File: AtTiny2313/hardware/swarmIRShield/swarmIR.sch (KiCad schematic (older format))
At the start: 32 parts, among them P1 CONN_2, P2 CONN_6, P3 CONN_2, P4 CONN_6, P5 CONN_2, P6 CONN_6, P7 CONN_2, P8 CONN_6, Q1 MOSFET_N, U1 TSOP1838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

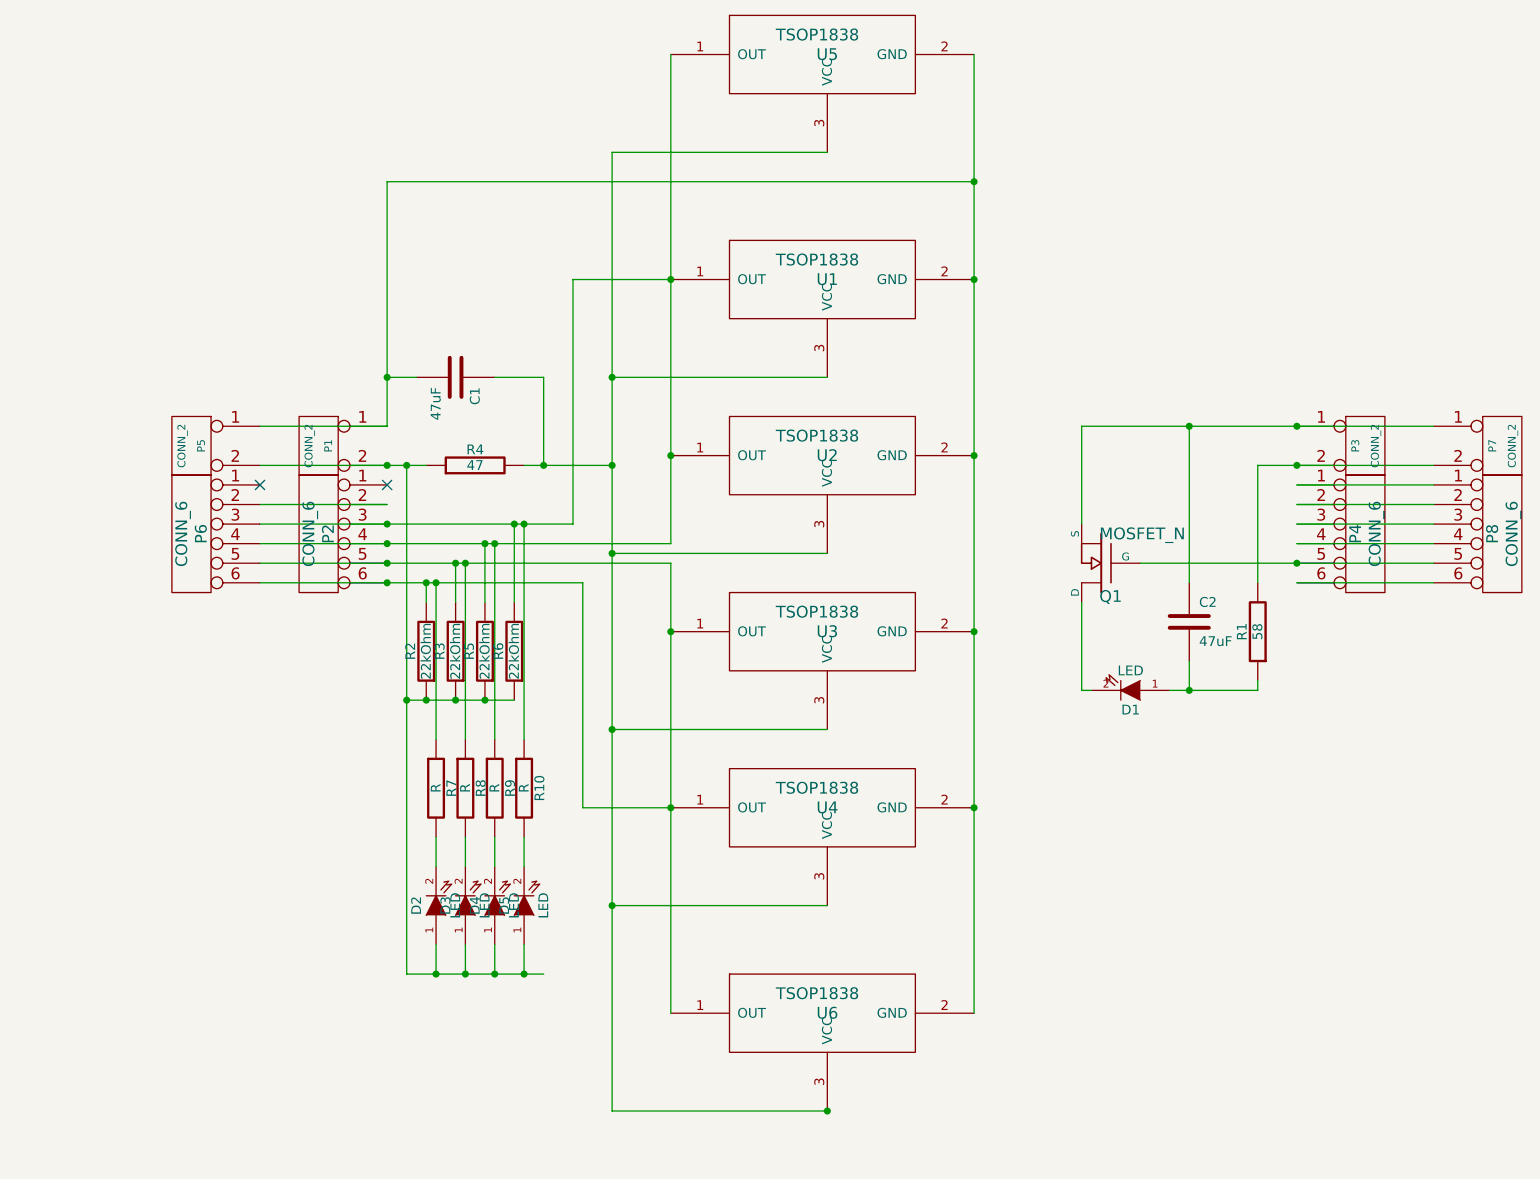
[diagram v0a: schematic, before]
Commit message: Added code comments 4/8MHz fuses, updated IR shield graphics
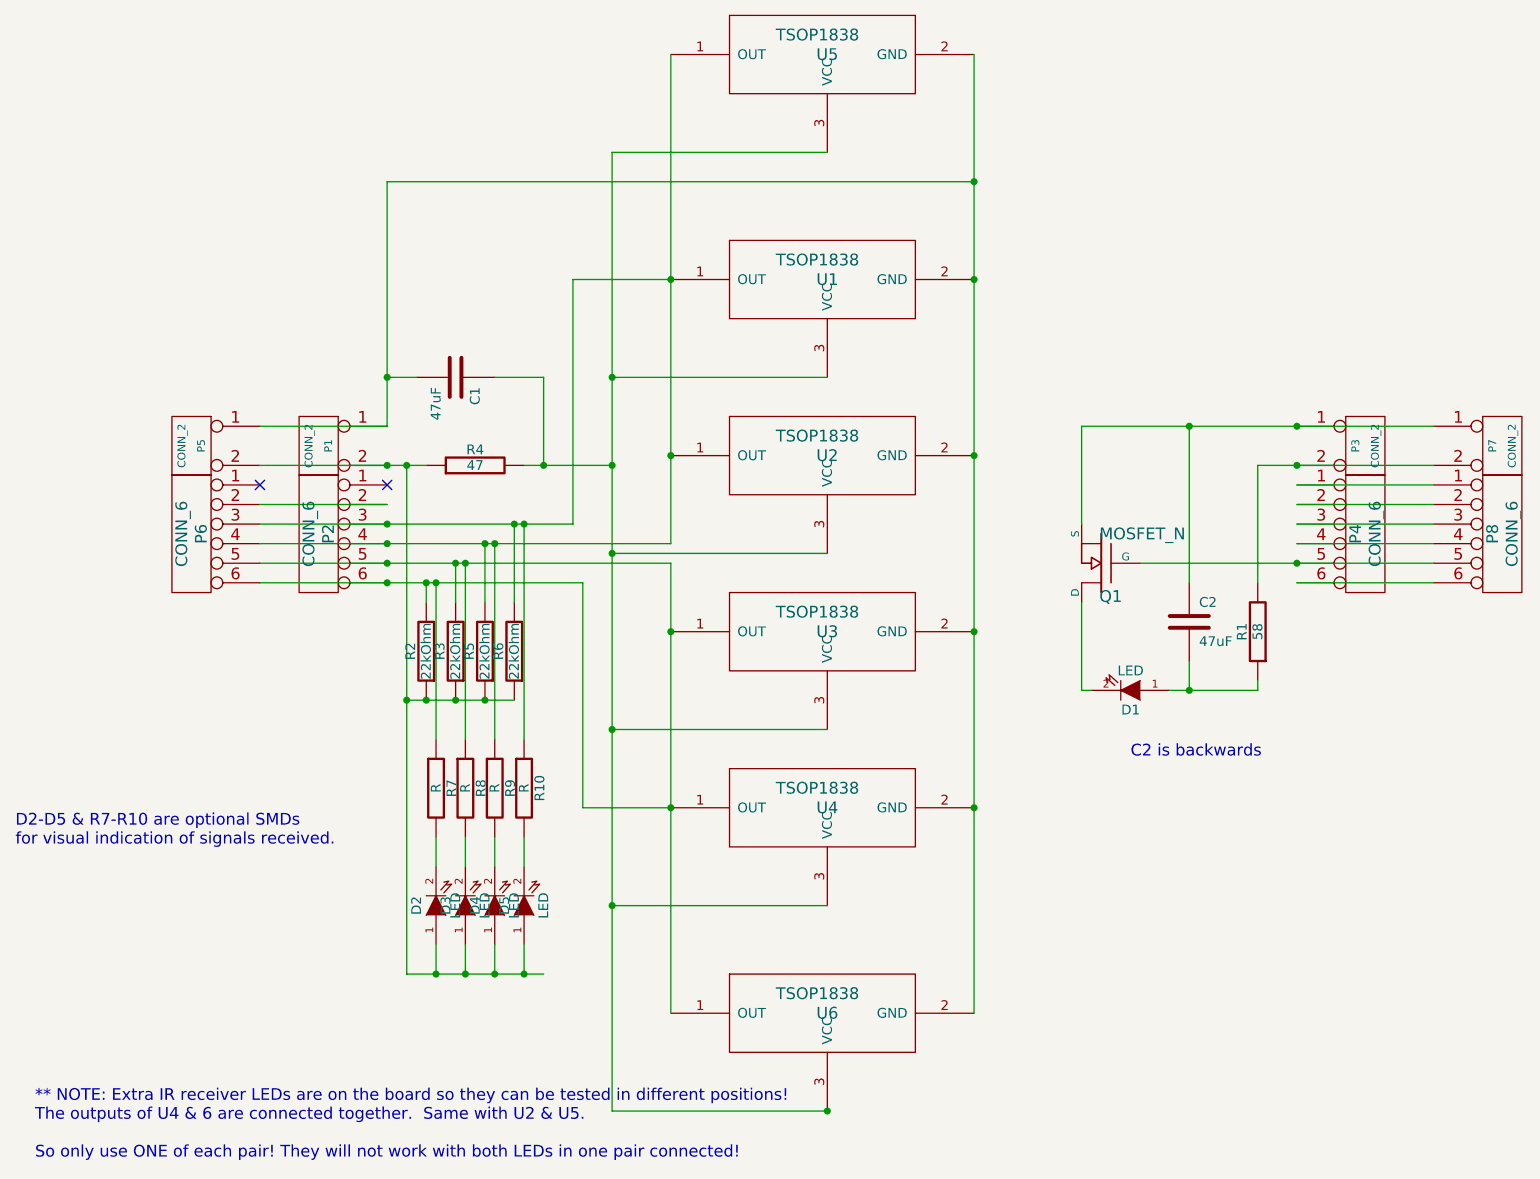
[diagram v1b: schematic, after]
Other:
- note added: "** NOTE: Extra IR receiver LEDs are on the board so they can be tested in different positions!\nThe outputs of U4 & 6 are connected together. Same with U2 & U5.\n\nSo only use ONE of each pair! They will not work with both LEDs in one pair connected!"
- note added: "C2 is backwards"
- note added: "D2-D5 & R7-R10 are optional SMDs\nfor visual indication of signals received."
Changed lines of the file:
@@
-EESchema Schematic File Version 2  date Thu 18 Oct 2012 08:24:53 CST
+EESchema Schematic File Version 2  date Fri 26 Oct 2012 22:03:20 CST
 LIBS:power
 LIBS:device
@@
 Sheet 1 1
 Title ""
-Date "18 oct 2012"
+Date "26 oct 2012"
 Rev ""
 Comp ""
@@
 Wire Wire Line
 	2950 4500 3500 4500
+Text Notes 1050 6850 0    60   ~ 0
+** NOTE: Extra IR receiver LEDs are on the board so they can be tested in different positions!\nThe outputs of U4 & 6 are connected together.  Same with U2 & U5.\n\nSo only use ONE of each pair! They will not work with both LEDs in one pair connected!
+Text Notes 950  5250 0    60   ~ 0
+D2-D5 & R7-R10 are optional SMDs\nfor visual indication of signals received.
+Text Notes 6650 4800 0    60   ~ 0
+C2 is backwards
 $EndSCHEMATC
